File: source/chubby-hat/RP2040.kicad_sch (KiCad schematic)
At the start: 23 parts, among them U4 P25Q40H-SSH-IT, U5 RP2040, Y1 12M

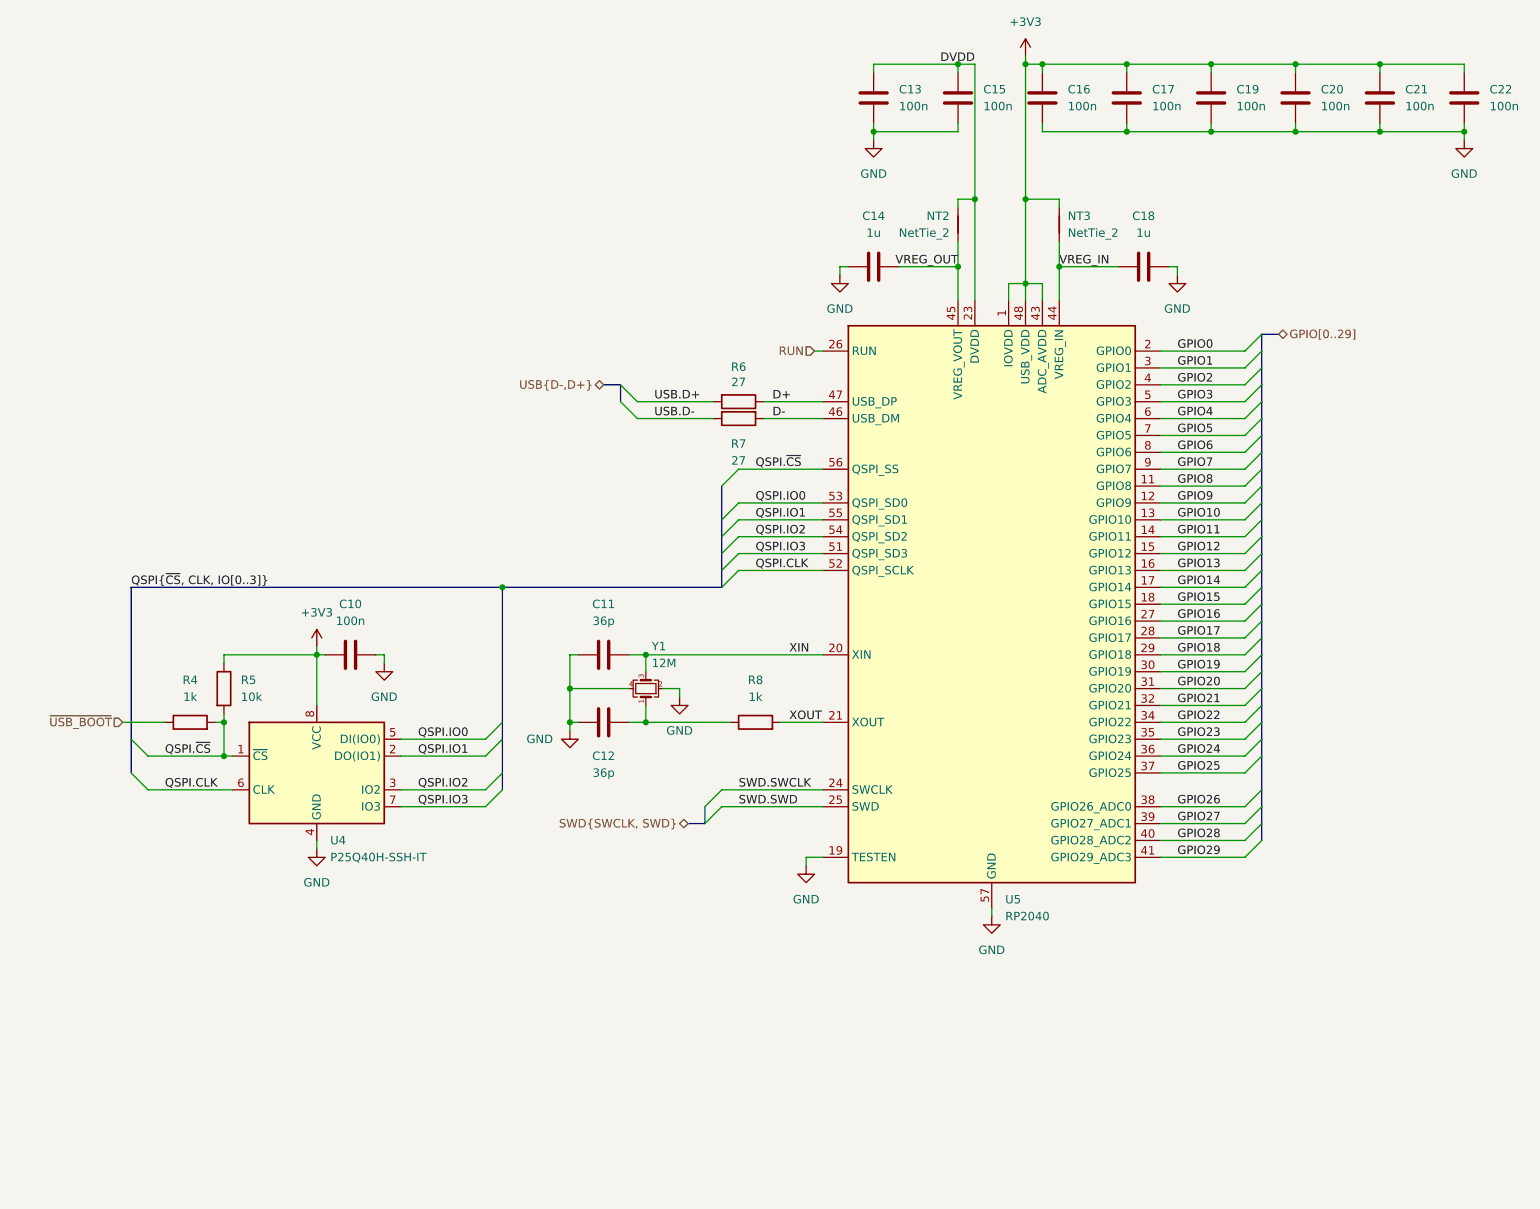
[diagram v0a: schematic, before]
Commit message: added connectors for v8.0; improved power layout
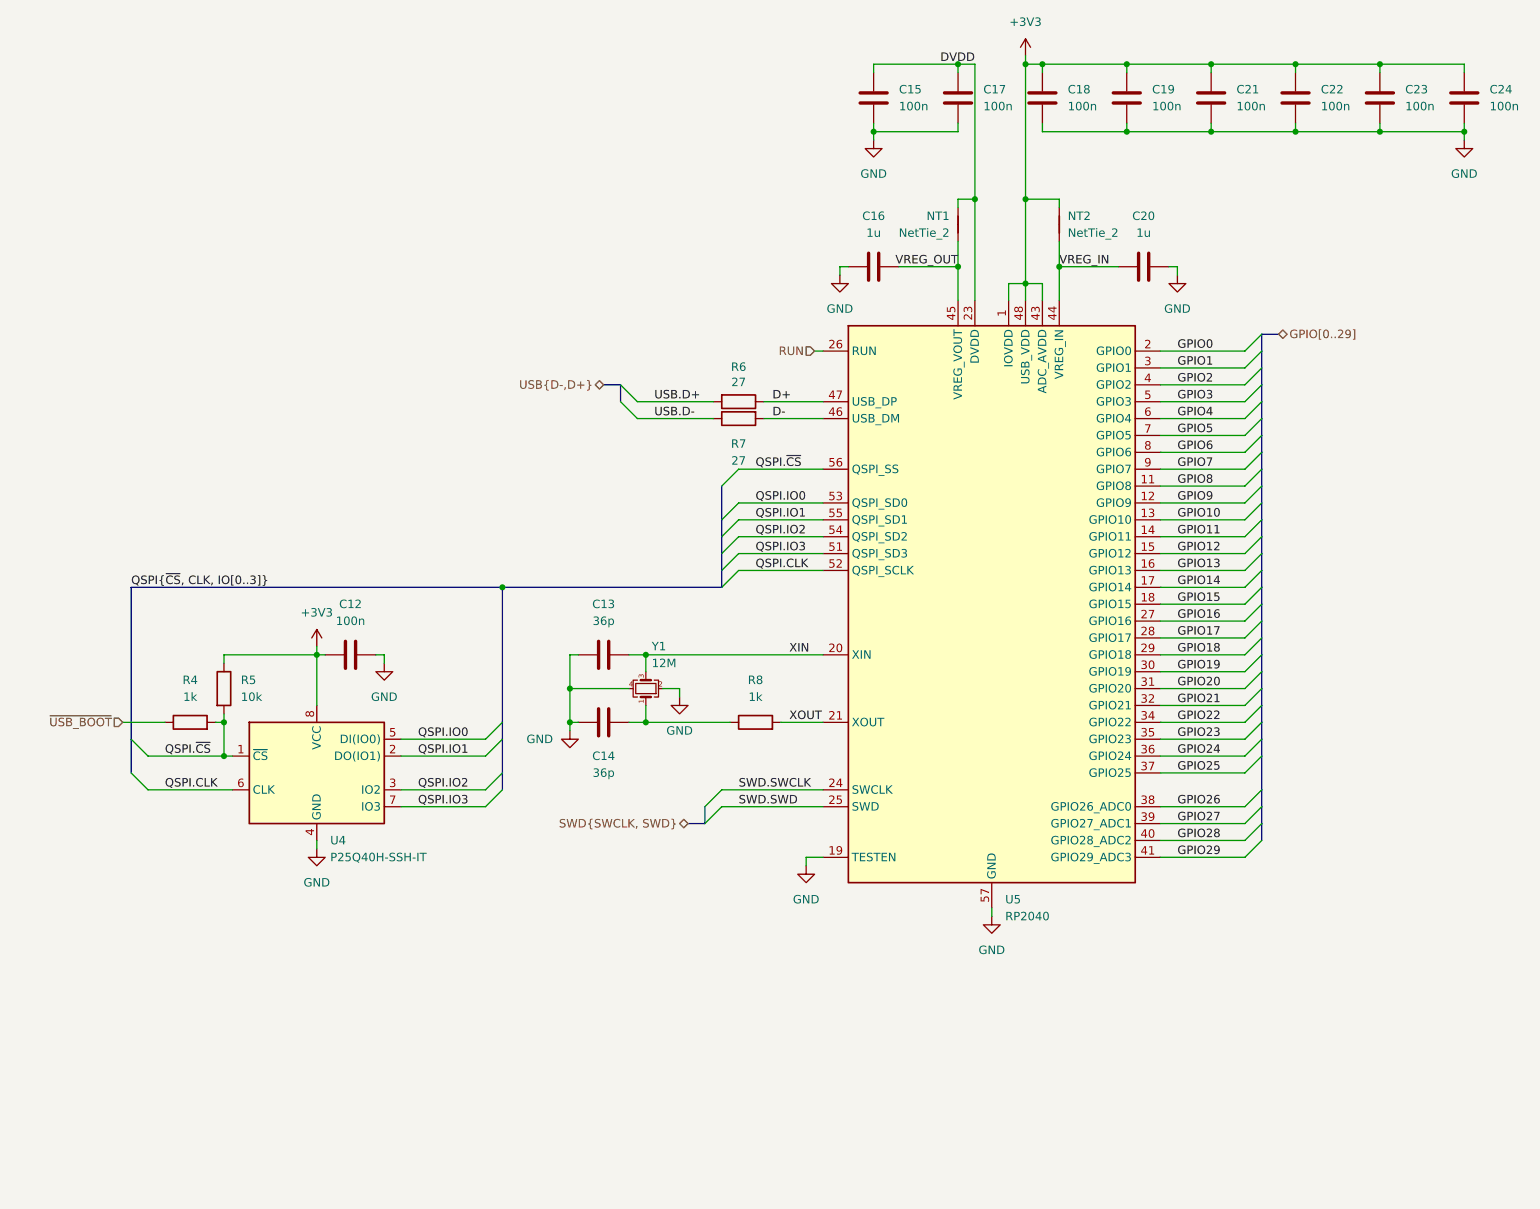
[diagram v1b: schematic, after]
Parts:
- renumbered C10 to C12, C11 to C13, C12 to C14, C13 to C15, C14 to C16, C15 to C17, C16 to C18, C17 to C19, C18 to C20, C19 to C21, C20 to C22, C21 to C23, C22 to C24, NT2 to NT1, NT3 to NT2
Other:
- title: (none) -> ${title}
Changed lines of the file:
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@@
   (paper "A4")
   (title_block
-    (date "2020-08-29")
+    (title "${title}")
+    (date "2023-01-29")
+    (rev "${revision}")
+    (comment 1 "${repo}")
   )
   (junction (at 175.26 25.4) (diameter 0) (color 0 0 0 0)
@@
   (symbol (lib_id "power:GND") (at 241.3 36.83 0) (unit 1)
     (in_bom yes) (on_board yes) (fields_autoplaced)
-    (property "Reference" "#PWR092" (id 0) (at 241.3 43.18 0)
+    (property "Reference" "#PWR093" (id 0) (at 241.3 43.18 0)
       (effects (font (size 1.27 1.27)) hide)
     )
@@
   (symbol (lib_id "Device:C") (at 73.66 114.3 90) (unit 1)
     (in_bom yes) (on_board yes) (fields_autoplaced)
-    (property "Reference" "C10" (id 0) (at 73.66 106.68 90))
+    (property "Reference" "C12" (id 0) (at 73.66 106.68 90))
     (property "Value" "100n" (id 1) (at 73.66 109.22 90))
     (property "Footprint" "Capacitor_SMD:C_0603_1608Metric" (id 2) (at 77.47 113.335 0)
@@
   (symbol (lib_id "Device:C") (at 152.4 30.48 0) (unit 1)
     (in_bom yes) (on_board yes) (fields_autoplaced)
-    (property "Reference" "C13" (id 0) (at 156.21 29.2099 0)
+    (property "Reference" "C15" (id 0) (at 156.21 29.2099 0)
       (effects (font (size 1.27 1.27)) (justify left))
     )
@@
   (symbol (lib_id "Device:NetTie_2") (at 165.1 49.53 90) (unit 1)
     (in_bom yes) (on_board yes) (fields_autoplaced)
-    (property "Reference" "NT2" (id 0) (at 163.83 48.2599 90)
+    (property "Reference" "NT1" (id 0) (at 163.83 48.2599 90)
       (effects (font (size 1.27 1.27)) (justify left))
     )
@@
   (symbol (lib_id "Device:C") (at 190.5 30.48 0) (unit 1)
     (in_bom yes) (on_board yes) (fields_autoplaced)
-    (property "Reference" "C17" (id 0) (at 194.31 29.2099 0)
+    (property "Reference" "C19" (id 0) (at 194.31 29.2099 0)
       (effects (font (size 1.27 1.27)) (justify left))
     )
@@
   (symbol (lib_id "power:+3V3") (at 68.58 113.03 0) (unit 1)
     (in_bom yes) (on_board yes) (fields_autoplaced)
-    (property "Reference" "#PWR081" (id 0) (at 68.58 116.84 0)
+    (property "Reference" "#PWR082" (id 0) (at 68.58 116.84 0)
       (effects (font (size 1.27 1.27)) hide)
     )
@@
   (symbol (lib_id "power:GND") (at 68.58 143.51 0) (unit 1)
     (in_bom yes) (on_board yes) (fields_autoplaced)
-    (property "Reference" "#PWR082" (id 0) (at 68.58 149.86 0)
+    (property "Reference" "#PWR083" (id 0) (at 68.58 149.86 0)
       (effects (font (size 1.27 1.27)) hide)
     )
@@
   (symbol (lib_id "power:GND") (at 147.32 57.15 0) (unit 1)
     (in_bom yes) (on_board yes) (fields_autoplaced)
-    (property "Reference" "#PWR087" (id 0) (at 147.32 63.5 0)
+    (property "Reference" "#PWR088" (id 0) (at 147.32 63.5 0)
       (effects (font (size 1.27 1.27)) hide)
     )
@@
   (symbol (lib_id "Device:C") (at 228.6 30.48 0) (unit 1)
     (in_bom yes) (on_board yes) (fields_autoplaced)
-    (property "Reference" "C21" (id 0) (at 232.41 29.2099 0)
+    (property "Reference" "C23" (id 0) (at 232.41 29.2099 0)
       (effects (font (size 1.27 1.27)) (justify left))
     )
@@
   (symbol (lib_id "power:GND") (at 152.4 36.83 0) (unit 1)
     (in_bom yes) (on_board yes) (fields_autoplaced)
-    (property "Reference" "#PWR088" (id 0) (at 152.4 43.18 0)
+    (property "Reference" "#PWR089" (id 0) (at 152.4 43.18 0)
       (effects (font (size 1.27 1.27)) hide)
     )
@@
   (symbol (lib_id "power:GND") (at 78.74 115.57 0) (unit 1)
     (in_bom yes) (on_board yes) (fields_autoplaced)
-    (property "Reference" "#PWR083" (id 0) (at 78.74 121.92 0)
+    (property "Reference" "#PWR084" (id 0) (at 78.74 121.92 0)
       (effects (font (size 1.27 1.27)) hide)
     )
@@
   (symbol (lib_id "Device:C") (at 203.2 30.48 0) (unit 1)
     (in_bom yes) (on_board yes) (fields_autoplaced)
-    (property "Reference" "C19" (id 0) (at 207.01 29.2099 0)
+    (property "Reference" "C21" (id 0) (at 207.01 29.2099 0)
       (effects (font (size 1.27 1.27)) (justify left))
     )
@@
   (symbol (lib_id "power:+3V3") (at 175.26 24.13 0) (unit 1)
     (in_bom yes) (on_board yes) (fields_autoplaced)
-    (property "Reference" "#PWR090" (id 0) (at 175.26 27.94 0)
+    (property "Reference" "#PWR091" (id 0) (at 175.26 27.94 0)
       (effects (font (size 1.27 1.27)) hide)
     )
@@
   (symbol (lib_id "Device:C") (at 241.3 30.48 0) (unit 1)
     (in_bom yes) (on_board yes) (fields_autoplaced)
-    (property "Reference" "C22" (id 0) (at 245.11 29.2099 0)
+    (property "Reference" "C24" (id 0) (at 245.11 29.2099 0)
       (effects (font (size 1.27 1.27)) (justify left))
     )
@@
   (symbol (lib_id "Device:C") (at 152.4 55.88 270) (unit 1)
     (in_bom yes) (on_board yes) (fields_autoplaced)
-    (property "Reference" "C14" (id 0) (at 152.4 48.26 90))
+    (property "Reference" "C16" (id 0) (at 152.4 48.26 90))
     (property "Value" "1u" (id 1) (at 152.4 50.8 90))
     (property "Footprint" "Capacitor_SMD:C_0603_1608Metric" (id 2) (at 148.59 56.845 0)
@@
   (symbol (lib_id "Device:C") (at 165.1 30.48 0) (unit 1)
     (in_bom yes) (on_board yes) (fields_autoplaced)
-    (property "Reference" "C15" (id 0) (at 168.91 29.2099 0)
+    (property "Reference" "C17" (id 0) (at 168.91 29.2099 0)
       (effects (font (size 1.27 1.27)) (justify left))
     )
@@
   (symbol (lib_id "Device:C") (at 193.04 55.88 90) (unit 1)
     (in_bom yes) (on_board yes) (fields_autoplaced)
-    (property "Reference" "C18" (id 0) (at 193.04 48.26 90))
+    (property "Reference" "C20" (id 0) (at 193.04 48.26 90))
     (property "Value" "1u" (id 1) (at 193.04 50.8 90))
     (property "Footprint" "Capacitor_SMD:C_0603_1608Metric" (id 2) (at 196.85 54.915 0)
@@
   (symbol (lib_id "Device:C") (at 111.76 124.46 270) (mirror x) (unit 1)
     (in_bom yes) (on_board yes) (fields_autoplaced)
-    (property "Reference" "C12" (id 0) (at 111.76 129.54 90))
+    (property "Reference" "C14" (id 0) (at 111.76 129.54 90))
     (property "Value" "36p" (id 1) (at 111.76 132.08 90))
     (property "Footprint" "Capacitor_SMD:C_0603_1608Metric" (id 2) (at 107.95 123.495 0)
@@
   (symbol (lib_id "power:GND") (at 123.19 120.65 0) (unit 1)
     (in_bom yes) (on_board yes) (fields_autoplaced)
-    (property "Reference" "#PWR085" (id 0) (at 123.19 127 0)
+    (property "Reference" "#PWR086" (id 0) (at 123.19 127 0)
       (effects (font (size 1.27 1.27)) hide)
     )
@@
   (symbol (lib_id "power:GND") (at 170.18 153.67 0) (unit 1)
     (in_bom yes) (on_board yes) (fields_autoplaced)
-    (property "Reference" "#PWR089" (id 0) (at 170.18 160.02 0)
+    (property "Reference" "#PWR090" (id 0) (at 170.18 160.02 0)
       (effects (font (size 1.27 1.27)) hide)
     )
@@
   (symbol (lib_id "Device:C") (at 215.9 30.48 0) (unit 1)
     (in_bom yes) (on_board yes) (fields_autoplaced)
-    (property "Reference" "C20" (id 0) (at 219.71 29.2099 0)
+    (property "Reference" "C22" (id 0) (at 219.71 29.2099 0)
       (effects (font (size 1.27 1.27)) (justify left))
     )
@@
   (symbol (lib_id "Device:C") (at 177.8 30.48 0) (unit 1)
     (in_bom yes) (on_board yes) (fields_autoplaced)
-    (property "Reference" "C16" (id 0) (at 181.61 29.2099 0)
+    (property "Reference" "C18" (id 0) (at 181.61 29.2099 0)
       (effects (font (size 1.27 1.27)) (justify left))
     )
@@
   (symbol (lib_id "power:GND") (at 198.12 57.15 0) (unit 1)
     (in_bom yes) (on_board yes) (fields_autoplaced)
-    (property "Reference" "#PWR091" (id 0) (at 198.12 63.5 0)
+    (property "Reference" "#PWR092" (id 0) (at 198.12 63.5 0)
       (effects (font (size 1.27 1.27)) hide)
     )
@@
   (symbol (lib_id "power:GND") (at 106.68 125.73 0) (unit 1)
     (in_bom yes) (on_board yes) (fields_autoplaced)
-    (property "Reference" "#PWR084" (id 0) (at 106.68 132.08 0)
+    (property "Reference" "#PWR085" (id 0) (at 106.68 132.08 0)
       (effects (font (size 1.27 1.27)) hide)
     )
@@
   (symbol (lib_id "Device:C") (at 111.76 114.3 270) (mirror x) (unit 1)
     (in_bom yes) (on_board yes) (fields_autoplaced)
-    (property "Reference" "C11" (id 0) (at 111.76 106.68 90))
+    (property "Reference" "C13" (id 0) (at 111.76 106.68 90))
     (property "Value" "36p" (id 1) (at 111.76 109.22 90))
     (property "Footprint" "Capacitor_SMD:C_0603_1608Metric" (id 2) (at 107.95 113.335 0)
@@
   (symbol (lib_id "power:GND") (at 142.24 146.05 0) (unit 1)
     (in_bom yes) (on_board yes) (fields_autoplaced)
-    (property "Reference" "#PWR086" (id 0) (at 142.24 152.4 0)
+    (property "Reference" "#PWR087" (id 0) (at 142.24 152.4 0)
       (effects (font (size 1.27 1.27)) hide)
     )
@@
   (symbol (lib_id "Device:NetTie_2") (at 180.34 49.53 270) (unit 1)
     (in_bom yes) (on_board yes) (fields_autoplaced)
-    (property "Reference" "NT3" (id 0) (at 181.61 48.2599 90)
-      (effects (font (size 1.27 1.27)) (justify left))
-    )
+    (property "Reference" "NT2" (id 0) (at 181.61 48.2599 90)
+      (effects (font (size 1.27 1.27)) (justify left))
+    )
